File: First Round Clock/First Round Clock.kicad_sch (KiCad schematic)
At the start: 19 parts

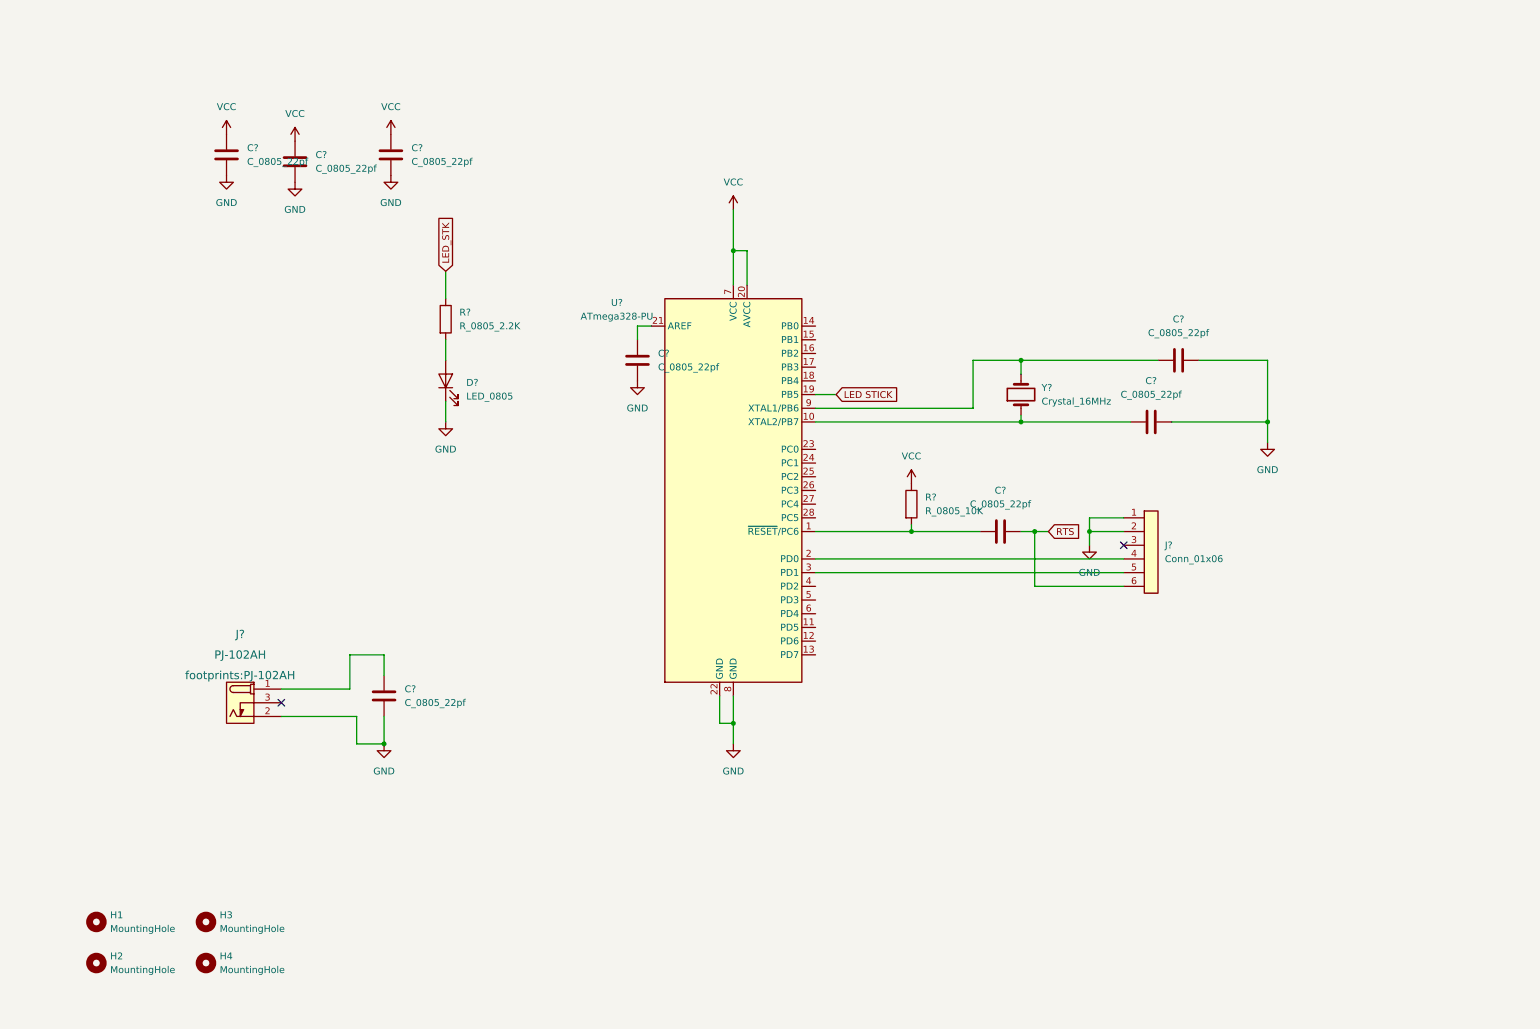
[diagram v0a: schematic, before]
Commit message: Week2
Blinking light with button and updated schematic
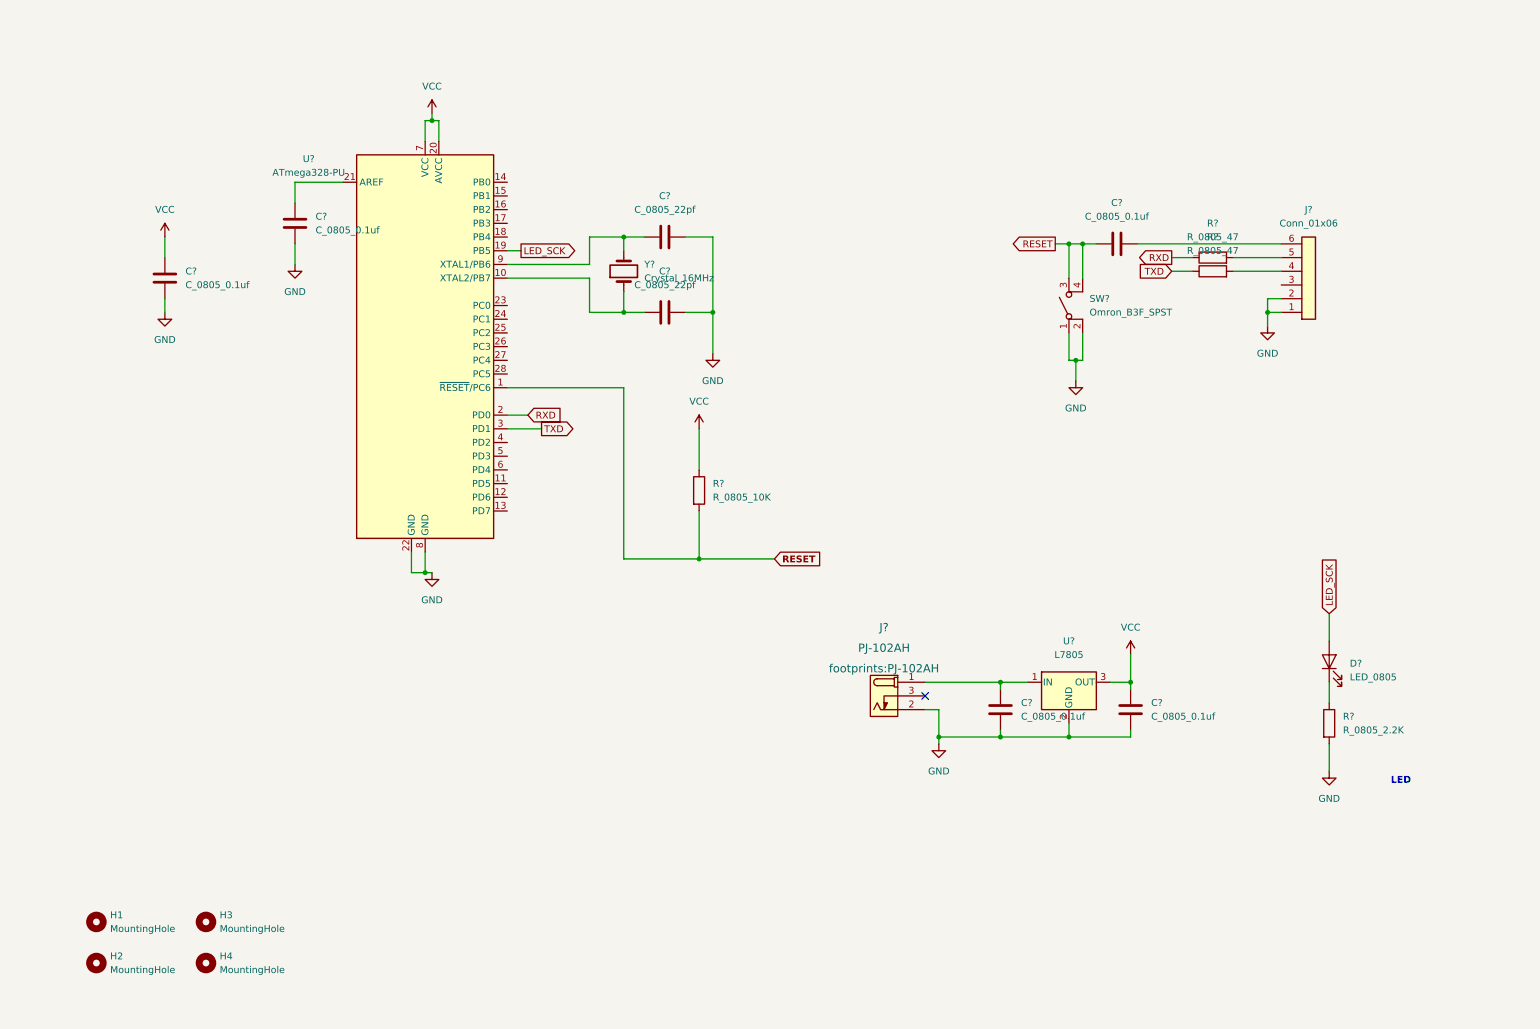
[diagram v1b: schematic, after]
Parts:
- removed C? (x8): C_0805_22pf, footprints:C_0805_2012Metric, symbol HPS:C_0805_22pf
- removed D?: LED_0805, footprints:LED_0805_2012Metric, symbol HPS:LED_0805
- removed J?: PJ-102AH, footprints:PJ-102AH, symbol HPS:PJ-102AH
- removed J?: Conn_01x06, footprints:PinHeader_1x06_P2.54mm_Vertical, symbol HPS:Conn_01x06
- removed R?: R_0805_2.2K, footprints:R_0805_2012Metric, symbol HPS:R_0805_2.2K
- removed R?: R_0805_10K, footprints:R_0805_2012Metric, symbol HPS:R_0805_10K
- removed U?: ATmega328-PU, footprints:DIP-28_W7.62mm, symbol HPS:ATmega328-PU
- removed Y?: Crystal_16MHz, footprints:Crystal_SMD_HC49-SD, symbol HPS:Crystal_16MHz
- added C? (x5): C_0805_0.1uf, footprints:C_0805_2012Metric, symbol HPS:C_0805_0.1uf
- added C? (x2): C_0805_22pf, footprints:C_0805_2012Metric, symbol HPS:C_0805_22pf
- added D?: LED_0805, footprints:LED_0805_2012Metric, symbol HPS:LED_0805
- added J?: Conn_01x06, footprints:PinHeader_1x06_P2.54mm_Vertical, symbol HPS:Conn_01x06
- added J?: PJ-102AH, footprints:PJ-102AH, symbol HPS:PJ-102AH
- added R? (x2): R_0805_47, footprints:R_0805_2012Metric, symbol HPS:R_0805_47
- added R?: R_0805_10K, footprints:R_0805_2012Metric, symbol HPS:R_0805_10K
- added R?: R_0805_2.2K, footprints:R_0805_2012Metric, symbol HPS:R_0805_2.2K
- added SW?: Omron_B3F_SPST, footprints:SW_SPST_Omron_B3FS-100xP, symbol HPS:Omron_B3F_SPST
- added U?: ATmega328-PU, footprints:DIP-28_W7.62mm, symbol HPS:ATmega328-PU
- added U?: L7805, symbol HPS:L7805
- added Y?: Crystal_16MHz, footprints:Crystal_SMD_HC49-SD, symbol HPS:Crystal_16MHz
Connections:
- net GND: now also C?.1, C?.2, C?.2, C?.2, C?.2, C?.2, J?.1 (Pin_1), J?.2 (OUT), J?.2 (Pin_2), R?.2, SW?.1 (A), SW?.2 (A), U?.2 (GND), U?.22 (GND), U?.8 (GND)
- net VCC: now also C?.1, C?.1, R?.1, U?.20 (AVCC), U?.3 (OUT), U?.7 (VCC)
- new net: C?.2, J?.6 (Pin_6)
- new net: C?.1, J?.1 (POLE), U?.1 (IN)
- new net: J?.5 (Pin_5), R?.2
- new net: C?.1, U?.10 (XTAL2/PB7), Y?.1
- new net: C?.1, U?.21 (AREF)
- new net: C?.2, U?.9 (XTAL1/PB6), Y?.2
- new net: J?.4 (Pin_4), R?.2
- new net: D?.1 (K), R?.1
- new net LED_SCK: D?.2 (A), U?.19 (PB5)
- new net RESET: C?.1, R?.2, SW?.3 (B), SW?.4 (B), U?.1 (~{RESET}/PC6)
- new net RXD: R?.1, U?.2 (PD0)
- new net TXD: R?.1, U?.3 (PD1)
- no-connect marks 2 -> 1
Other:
- note added: "LED"

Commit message: Week 3 deliverables
updated schematic and clock  code
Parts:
- added DS?: TC1602A-01T, footprints:TC1602A-01T, symbol HPS:TC1602A-01T
- added Q? (x2): US5881, footprints:TO-92S, symbol HPS:US5881
- added SW? (x3): Omron_B3F_SPST, footprints:SW_SPST_Omron_B3FS-100xP, symbol HPS:Omron_B3F_SPST
- added U?: DS1307_DIP-8, footprints:DIP-8_W7.62mm, symbol HPS:DS1307_DIP-8

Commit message: Week 4
Final schematic update hopefully
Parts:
- removed C?: C_0805_0.1uf, footprints:C_0805_2012Metric, symbol HPS:C_0805_0.1uf
- removed Q? (x2): US5881, footprints:TO-92S, symbol HPS:US5881
- removed SW?: Omron_B3F_SPST, footprints:SW_SPST_Omron_B3FS-100xP, symbol HPS:Omron_B3F_SPST
- added BT?: Battery_Cell, footprints:BatteryHolder_Keystone_106_1x20mm, symbol HPS:Battery_Cell
- added J?: Conn_02x03_Odd_Even, footprints:PinHeader_2x03_P2.54mm_Vertical, symbol HPS:Conn_02x03_Odd_Even
- added R? (x2): R_0805_4.7K, footprints:R_0805_2012Metric, symbol HPS:R_0805_4.7K
- added R?: R_0805_100K, footprints:R_0805_2012Metric, symbol HPS:R_0805_100K
- added R? (x3): R_0805_10K, footprints:R_0805_2012Metric, symbol HPS:R_0805_10K
- added R?: PhotoconductivePhotocell, footprints:R_LDR_4.9x4.2mm_P2.54mm_Vertical, symbol HPS:PhotoconductivePhotocell
- added RV?: R_POT_10K, footprints:Potentiometer_Bourns_3386P_Vertical, symbol HPS:R_POT_10K
- added SW?: Omron_B3F_SPST, footprints:SW_SPST_Omron_B3FS-100xP, symbol HPS:Omron_B3F_SPST
- added Y?: Crystal_32768Hz, footprints:Crystal_SMD_2Pin_3.2x1.5mm, symbol HPS:Crystal_32768Hz
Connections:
- net GND: now also DS?.1 (VSS), DS?.16 (LED(-)), DS?.5 (R/W), SW?.1 (A), SW?.1 (A), SW?.2 (A), SW?.2 (A), U?.4 (GND), BT?.2 (-), J?.6 (Pin_6), R?.2, RV?.3, SW?.1 (A), SW?.2 (A)
- net LED_SCK: now also J?.3 (Pin_3)
- net RESET: now also J?.5 (Pin_5)
- net VCC: now also DS?.15 (LED(+)), U?.8 (VCC), J?.2 (Pin_2), R?.1, R?.1, R?.1, R?.1, R?.1, R?.2, RV?.1
- net at U?.1 (X1): now also Y?.2
- net at U?.2 (X2): now also Y?.1
- net at U?.3 (VBAT): now also BT?.1 (+)
- net SDA: now reaches U?.5 (SDA)
- net SDA: now also U?.27 (PC4), R?.1
- net SCL: now reaches U?.6 (SCL)
- net SCL: now also U?.28 (PC5), R?.2
- net BTN_UP: now reaches SW?.3 (B)
- net BTN_UP: now also SW?.4 (B), U?.6 (PD4), R?.2
- net LCD_11: now reaches U?.11 (PD5)
- net LCD_11: now also DS?.11 (D4)
- net LCD_12: now reaches U?.12 (PD6)
- net LCD_12: now also DS?.12 (D5)
- net LCD_13: now reaches U?.13 (PD7)
- net LCD_13: now also DS?.13 (D6)
- net LCD_14: now reaches U?.14 (PB0)
- net LCD_14: now also DS?.14 (D7)
- net LCD_4: now reaches U?.15 (PB1)
- net LCD_4: now also DS?.4 (RS)
- net LCD_6: now reaches U?.16 (PB2)
- net LCD_6: now also DS?.6 (E)
- net MOSI: now reaches U?.17 (PB3)
- net MOSI: now also J?.4 (Pin_4)
- net MISO: now reaches U?.18 (PB4)
- net MISO: now also J?.1 (Pin_1)
- net Light_Sensor: now reaches U?.23 (PC0)
- net BTN_MODE: now reaches U?.4 (PD2)
- net BTN_MODE: now also R?.2, SW?.3 (B), SW?.4 (B)
- net BTN_SEL: now reaches U?.5 (PD3)
- net BTN_SELECT: now reaches SW?.3 (B)
- net BTN_SELECT: now also SW?.4 (B), R?.2
- net at DS?.3 (VO): now also RV?.2
- new net LIGHT_SENSOR: R?.1, R?.2
- no-connect marks 1 -> 10
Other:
- moved on the sheet: C?, D?, DS?, J?, R?, SW?, U?, Y?

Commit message: Updated BOM and schematic
New and final BOM
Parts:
- removed J?: Conn_02x03_Odd_Even, footprints:PinHeader_2x03_P2.54mm_Vertical, symbol HPS:Conn_02x03_Odd_Even
- removed U?: L7805, symbol HPS:L7805
- added BZ1: Buzzer, footprints:Buzzer_TDK_PS1240P02BT_D12.2mm_H6.5mm, symbol HPS:Buzzer
- added Q1: NPN_2N3904_SOT23, footprints:SOT-23, symbol HPS:NPN_2N3904_SOT23
- added R11: R_0805_10K, footprints:R_0805_2012Metric, symbol HPS:R_0805_10K
- added R7: R_0805_2.2K, footprints:R_0805_2012Metric, symbol HPS:R_0805_2.2K
- added SW3: Omron_B3F_SPST, footprints:SW_SPST_Omron_B3FS-100xP, symbol HPS:Omron_B3F_SPST
- added U1: L7805, footprints:TO-220-3_Vertical, symbol HPS:L7805
- gave numbers to parts that had none: 31
- renumbered H3 to H2, H2 to H3
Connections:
- net GND: now also Q1.2 (E), SW3.1 (A), SW3.2 (A), U1.2 (GND)
- net VCC: now also DS1.2 (VDD), BZ1.1 (-), R11.1, U1.3 (OUT)
- net at C3.1, J1.1 (POLE): now also U1.1 (IN)
- net MISO renamed Buzz
- net Buzz: now also R7.1
- net MOSI: no longer names the net of U2.17 (PB3)
- new net: Q1.1 (B), R7.2
- new net: BZ1.2 (+), Q1.3 (C)
- new net BTN_DWN: R11.2, SW3.3 (B), SW3.4 (B)
